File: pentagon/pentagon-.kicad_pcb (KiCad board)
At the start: 2 copper layers, 80.9 x 76.9 mm, 28 parts, among them J1 Conn_01x05_Pin, J2 Conn_01x05_Pin, J3 Conn_01x05_Pin, J4 Conn_01x05_Pin, J5 Conn_01x05_Pin

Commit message: updated all coolness
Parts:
- removed C10, C2, C3, C4, C5, C6, C7, C8, C9: C, Capacitor_SMD:C_0805_2012Metric_Pad1.18x1.45mm_HandSolder
- added JP4: SolderJumper_2_Open, Jumper:SolderJumper-2_P1.3mm_Open_RoundedPad1.0x1.5mm, F.Cu at (78.4, 95.4)
- added JP5: SolderJumper_2_Open, Jumper:SolderJumper-2_P1.3mm_Open_RoundedPad1.0x1.5mm, F.Cu at (65.0, 54.0)
- added JP6: SolderJumper_2_Open, Jumper:SolderJumper-2_P1.3mm_Open_RoundedPad1.0x1.5mm, F.Cu at (100.0, 28.6)
- added JP7: SolderJumper_2_Open, Jumper:SolderJumper-2_P1.3mm_Open_RoundedPad1.0x1.5mm, F.Cu at (135.0, 54.6)
- added JP8: SolderJumper_2_Open, Jumper:SolderJumper-2_P1.3mm_Open_RoundedPad1.0x1.5mm, F.Cu at (121.6, 95.6)
- moved JP3 28.3 mm to (100.0, 26.0)
- moved JP2 27.7 mm to (62.8, 53.4), turned to 72 degrees
- moved JP1 27.2 mm to (137.0, 53.8), turned to -72 degrees
- moved D1 7.23 mm to (98.2, 86.0)
- moved D3 6.72 mm to (79.8, 70.6)
- moved D5 6.72 mm to (88.8, 48.2)
- moved D9 6.68 mm to (119.4, 73.0)
- moved D7 6.63 mm to (113.4, 49.6)
- moved C1 6.08 mm to (99.4, 89.8), turned to 180 degrees
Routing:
- net GND: track 342.7 -> 672.9 mm
- net Net-(J2-Pin_3): track 46.9 -> 23.3 mm
- net Net-(D1-DIN): track 7.58 -> 14.3 mm
- net Net-(D6-DOUT): track 17.2 -> 23.0 mm
- net Net-(D2-DOUT): track 17.7 -> 22.9 mm
- net Net-(D4-DOUT): track 18.0 -> 23.2 mm
- net Net-(D8-DOUT): track 18.0 -> 22.7 mm
- net Net-(J4-Pin_3): track 43.2 -> 47.8 mm
- net Net-(D10-DIN): track 21.0 -> 22.8 mm
- net Net-(J5-Pin_3): track 45.9 -> 47.4 mm
- net Net-(D10-DOUT): track 49.7 -> 50.9 mm
- net +5V: track 455.0 -> 455.7 mm
- net Net-(D3-DOUT): track 23.9 -> 23.4 mm
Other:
- outline, holes or cut-outs redrawn

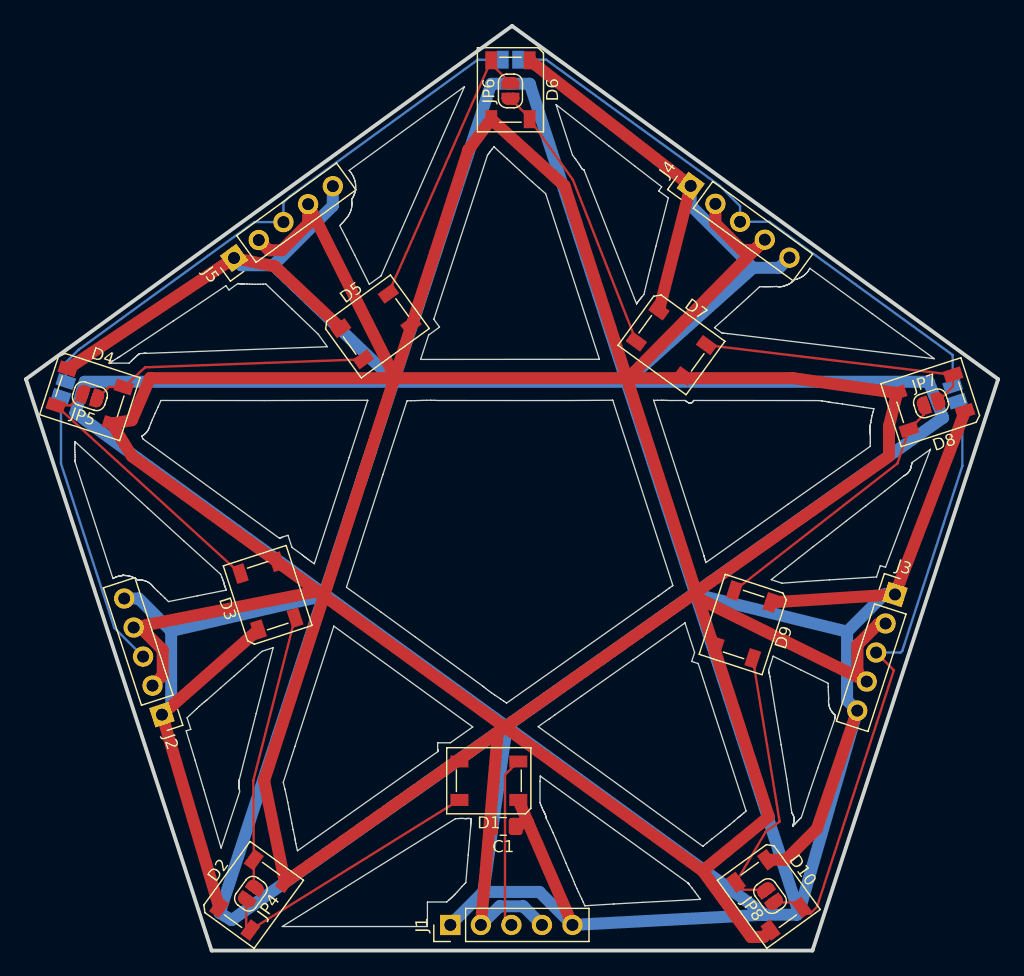
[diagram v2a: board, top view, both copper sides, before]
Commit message: added mic to antenna, decagons, octagons and all the shenanigans
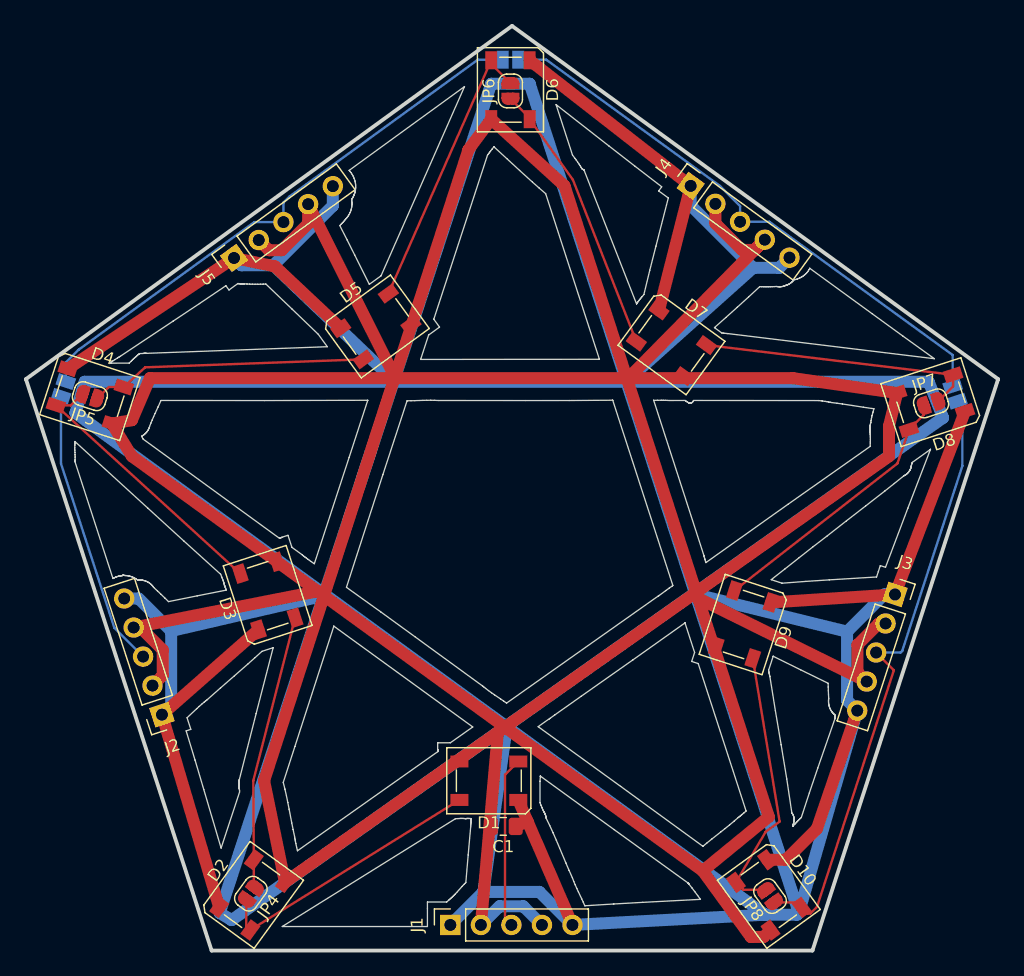
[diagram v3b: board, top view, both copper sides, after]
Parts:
- J1, J2, J3, J4, J5: footprint Connector_PinHeader_2.54mm:PinHeader_1x05_P2.54mm_Vertical -> Connector_PinSocket_2.54mm:PinSocket_1x05_P2.54mm_Vertical
